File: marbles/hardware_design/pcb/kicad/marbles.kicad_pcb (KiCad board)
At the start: 2 copper layers, 88.9 x 106 mm, 222 parts, among them IC1 R-78E3.3-0.5, IC10 TL074PW, IC2 STM32F405RGT6, IC3 LD2981ABU33, IC4 DAC8164ICPW, IC5 MCP6004, IC6 MCP6004, IC7 OPA4171, IC8 LM4040B10, IC9 LM324PW, J1 PJ301_THONKICONN6, J10 PJ301_THONKICONN6, J11 PJ301_THONKICONN6, J12 PJ301_THONKICONN6, J13 PJ301_THONKICONN6, J14 PJ301_THONKICONN6, J15 PJ301_THONKICONN6, J16 PJ301_THONKICONN6, J2 PJ301_THONKICONN6, J3 PJ301_THONKICONN6, J4 PJ301_THONKICONN6, J5 PJ301_THONKICONN6, J6 PJ301_THONKICONN6, J7 PJ301_THONKICONN6, J8 PJ301_THONKICONN6, J9 PJ301_THONKICONN6, Q1 8MHz, Q2 MMBT3904, Q3 MMBT3904, SW1 SW_Push_LED, SW2 SW_Push_LED, SW3 TAC_SWITCHPTH, SW4 TAC_SWITCHPTH, SW5 TAC_SWITCHPTH, SW6 TAC_SWITCHPTH, SW7 TAC_SWITCHPTH

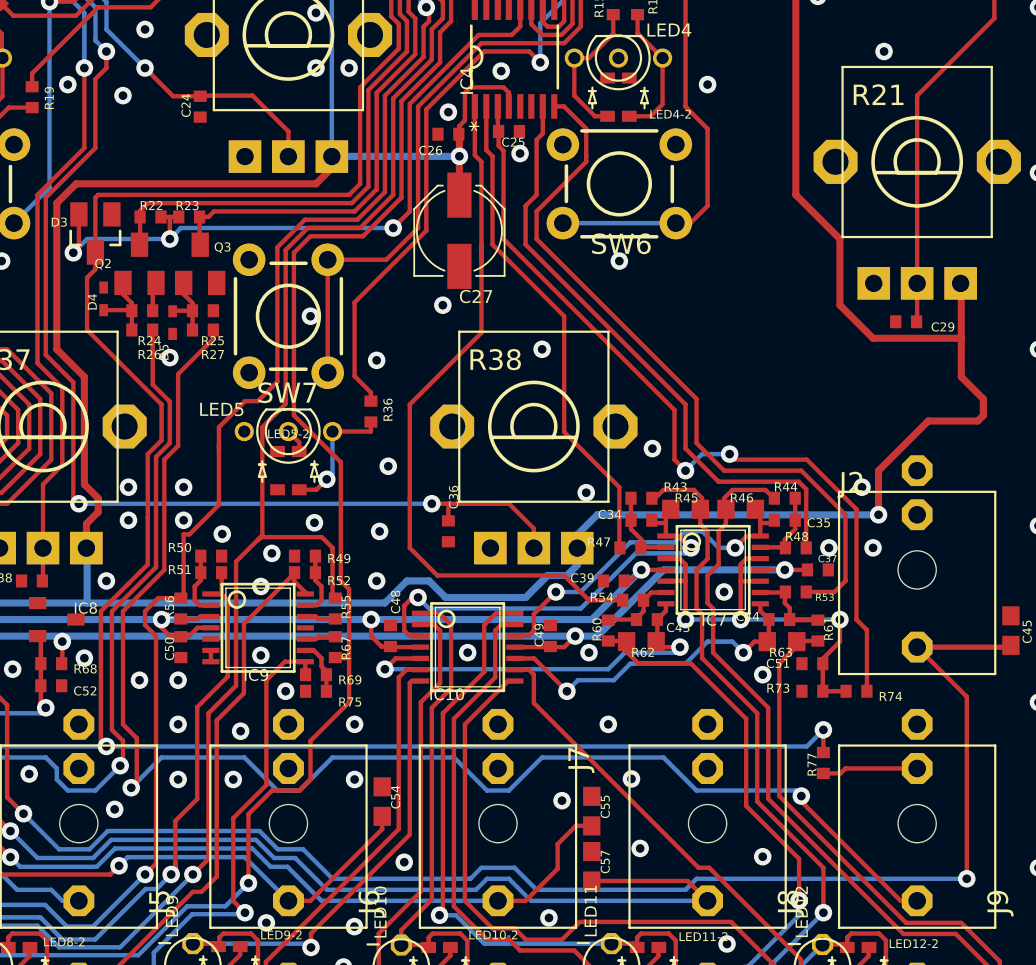
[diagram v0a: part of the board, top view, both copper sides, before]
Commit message: changed opa4174 package
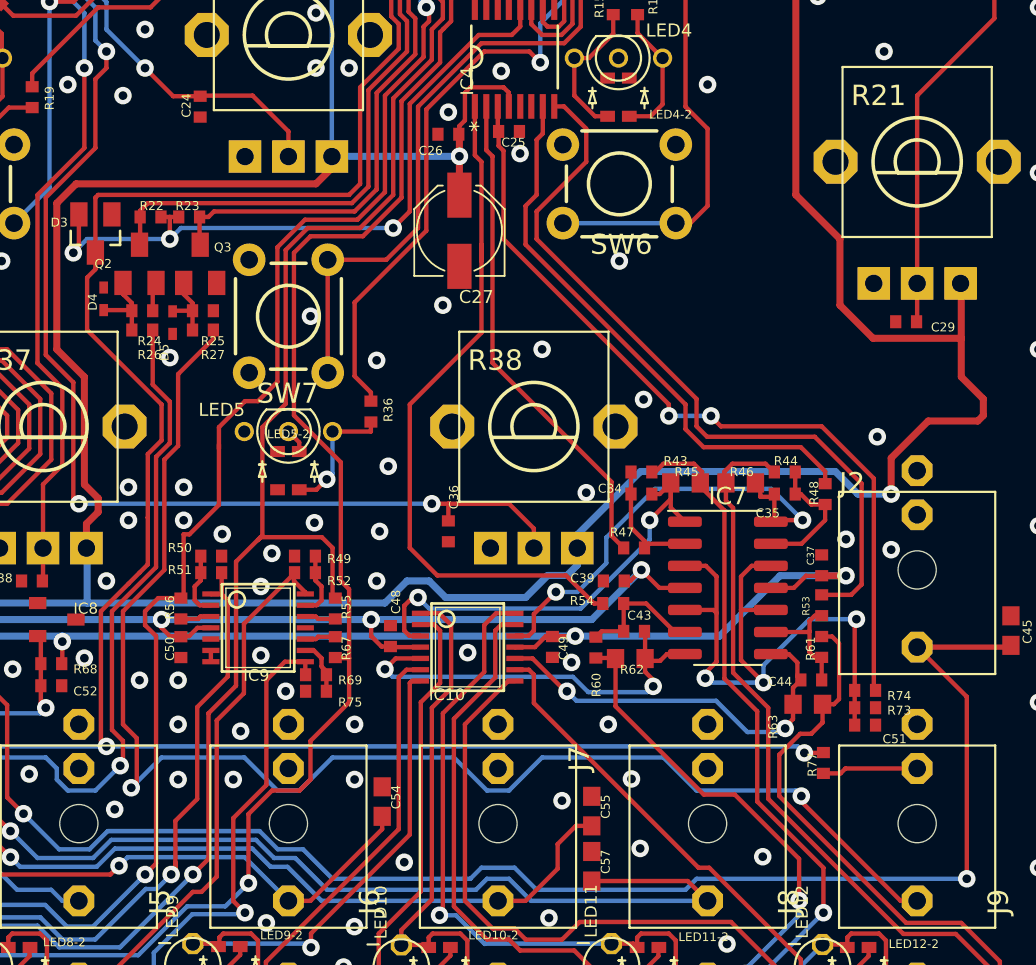
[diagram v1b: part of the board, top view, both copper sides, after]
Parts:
- IC7: footprint marbles:TSSOP14_065 -> Package_SO:SO-14_3.9x8.65mm_P1.27mm
- moved C51 4.66 mm to (181.7, 131.4), turned to 0 degrees
- moved C44 3.93 mm to (178.6, 128.8)
- moved R63 3.90 mm to (178.4, 130.2)
- moved R48 3.53 mm to (179.4, 118.1), turned to 90 degrees
- moved R73 3.18 mm to (181.7, 130.4), turned to 180 degrees
- moved R53 1.67 mm to (179.2, 124.5), turned to 90 degrees
- moved R45 1.51 mm to (171.4, 117.5)
- moved R46 1.51 mm to (174.5, 117.5)
- moved C34 1.51 mm to (168.8, 118.1)
- moved C35 1.51 mm to (177.1, 118.1)
- moved R43 1.51 mm to (168.8, 116.8)
- moved R44 1.51 mm to (177.1, 116.8)
- moved IC7 1.34 mm to (173.8, 123.5), turned to 0 degrees
- moved R60 1.21 mm to (166.2, 126.9)
- moved R62 1.17 mm to (168.2, 127.6)
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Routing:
- net /marbles_5/VREF_BIAS: track 25.9 -> 37.5 mm
- net Net-(C35-Pad2): track 20.4 -> 26.8 mm
- net VEE: track 122.7 -> 127.9 mm
- net Net-(C44-Pad2): track 19.4 -> 23.4 mm
- net Net-(C35-Pad1): track 4.58 -> 7.83 mm
- net Net-(C43-Pad1): track 4.42 -> 7.54 mm
- net DAC_X_2: track 35.2 -> 32.6 mm
- net Net-(C34-Pad1): track 4.61 -> 7.12 mm
- net Net-(C44-Pad1): track 4.86 -> 6.99 mm
- net DAC_X_3: track 42.1 -> 43.7 mm
- net Net-(C34-Pad2): track 25.2 -> 26.8 mm
- net Net-(J16-PadP3): track 41.8 -> 43.3 mm
- net NORMALIZATION_PROBE: track 133.0 -> 131.4 mm
- net VCC: track 134.5 -> 136.0 mm
- net Net-(J15-PadP3): track 65.4 -> 66.8 mm
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
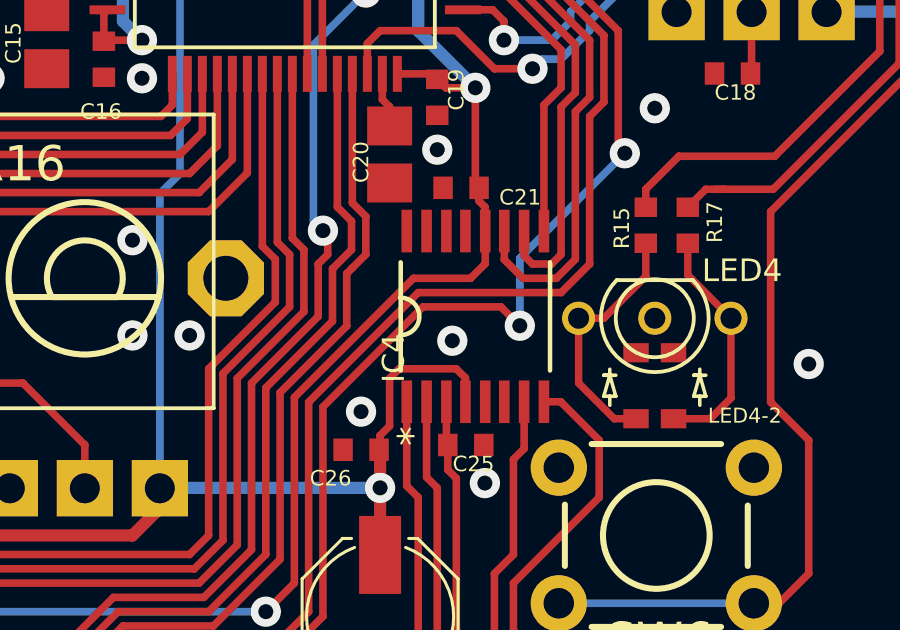
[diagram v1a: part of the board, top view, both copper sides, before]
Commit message: change dac from 8164 to 8565
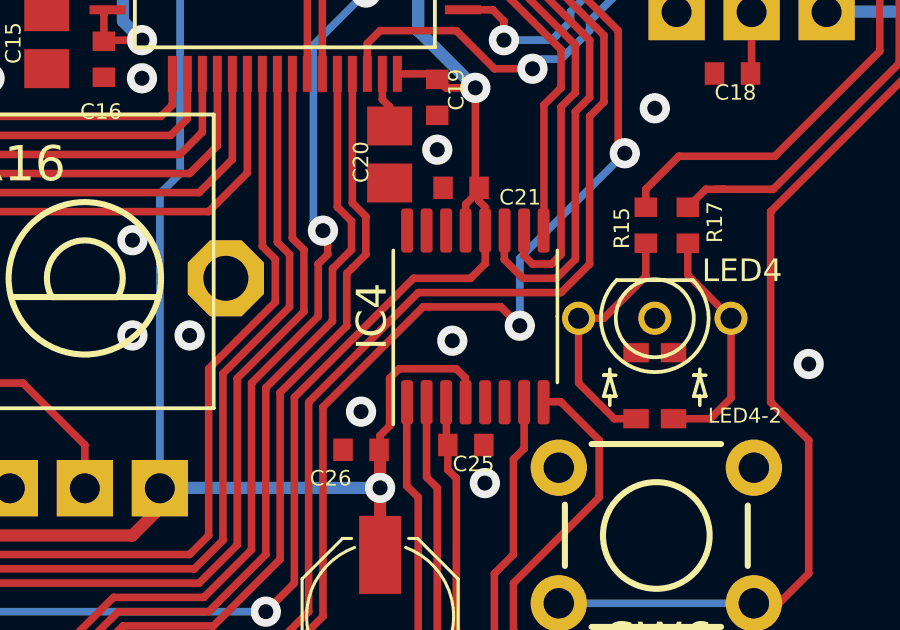
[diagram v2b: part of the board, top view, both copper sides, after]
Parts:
- IC4: value DAC8164ICPW -> DAC8565; footprint marbles:SOP65P640X110-16N -> Package_SO:TSSOP-16_4.4x5mm_P0.65mm
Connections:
- IC4 pad 13: GND -> +3V3
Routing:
- net +3V3: track 202.2 -> 203.8 mm

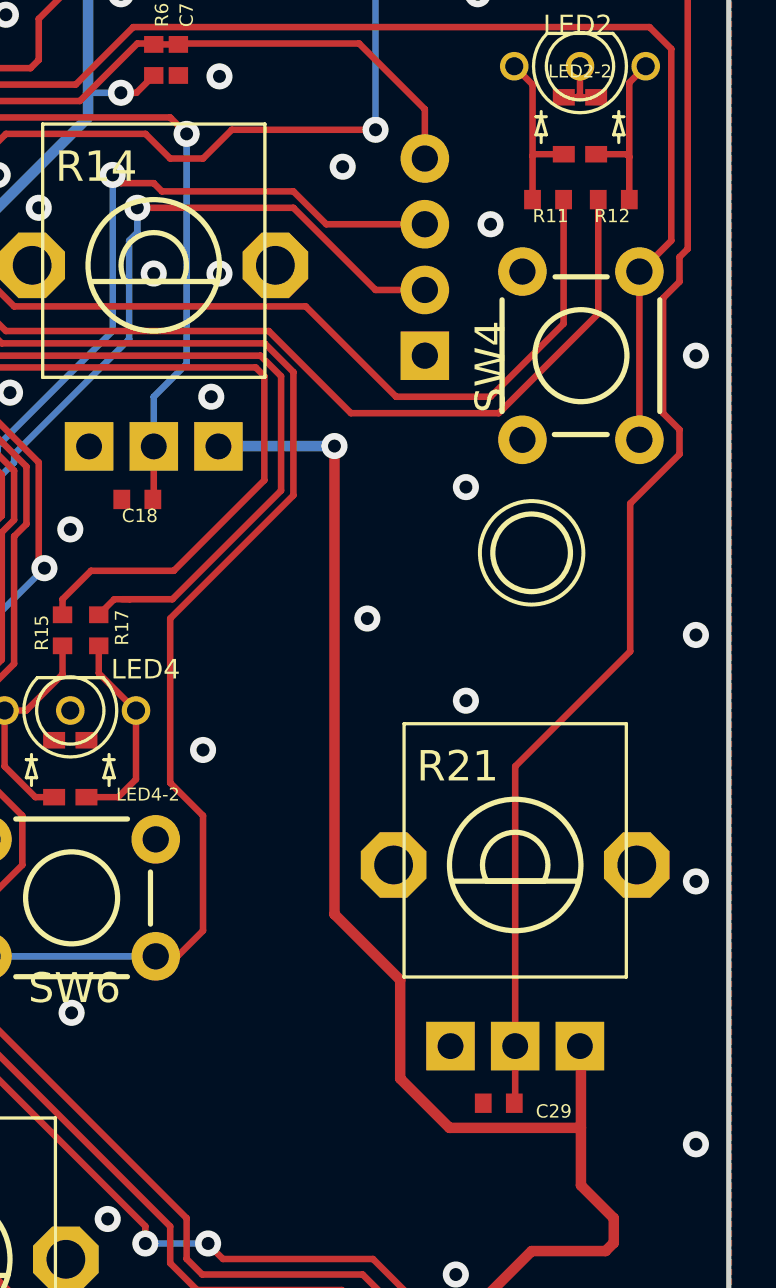
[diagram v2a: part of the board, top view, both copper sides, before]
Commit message: add smd flash header in parallel
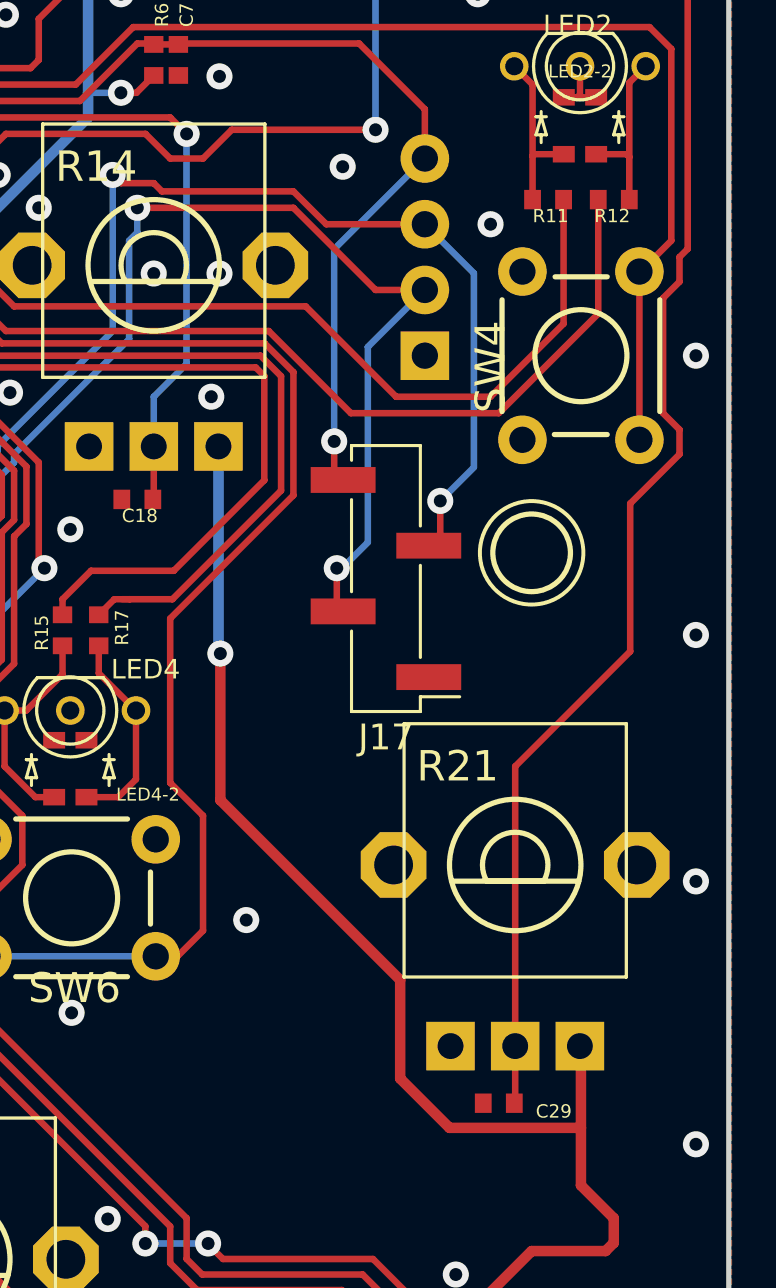
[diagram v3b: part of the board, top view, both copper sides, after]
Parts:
- added J17: Conn_01x04_Male, Connector_PinHeader_2.54mm:PinHeader_1x04_P2.54mm_Vertical_SMD_Pin1Left, F.Cu at (179.7, 87.9)
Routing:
- net /marbles_2/SWDIO: track 33.9 -> 47.9 mm, vias 2 -> 3
- net /marbles_2/RESET: track 32.3 -> 46.3 mm, vias 0 -> 1
- net /marbles_2/SWCLK: track 30.1 -> 44.1 mm, vias 2 -> 3
- net +3V3_A: track 302.9 -> 300.2 mm
- net GND: vias 158 -> 155
